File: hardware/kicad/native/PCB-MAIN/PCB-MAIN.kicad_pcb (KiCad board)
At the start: 6 copper layers, 110 x 75 mm, 251 parts, among them J10 U.FL-R-SMT-1(60), J11 USB4105-GF-A-120, J12 MEM2052-00-195-00-A, J13 504050-0291, J6 2336582-1, J7 2336582-1, J8 U.FL-R-SMT-1(60), J9 U.FL-R-SMT-1(60), Q1 MMBT3904,215, Q2 MMBT3904,215, Q3 MMBT3904,215, Q4 Si1016X-T1-GE3, U1 STM32U585VIT6Q, U10 E22-900M22S, U11 MDBT50Q-P1MV2, U13 TS3A27518EPWR, U14 ESDALC6V1-5P6, U15 ESDALC6V1-5P6, U16 SN74AXC8T245PWR, U17 SN74LVC32APWR, U18 SN74AXC1T45DRLR, U19 TPD4E05U06DQAR, U2 W25Q512JVFIQ, U20 TPD4E05U06DQAR, U21 TPD4E05U06DQAR, U22 TPD4E05U06DQAR, U23 TPD4E05U06DQAR, U24 TPD4E05U06DQAR, U25 TPD2EUSB30DRTR, U26 TPD2EUSB30DRTR, U27 TPD4E05U06DQAR, U3 LIS2DW12TR, U4 STTS22HTR, U5 LT6000IDCB#TRMPBF, U6 SN74LVC1G07DBVR, U7 SN74AXC8T245PWR, U8 BG95-M3, U9 MAX-M10S-00B, X1 SiT1552AI-JE-DCC-32.768D

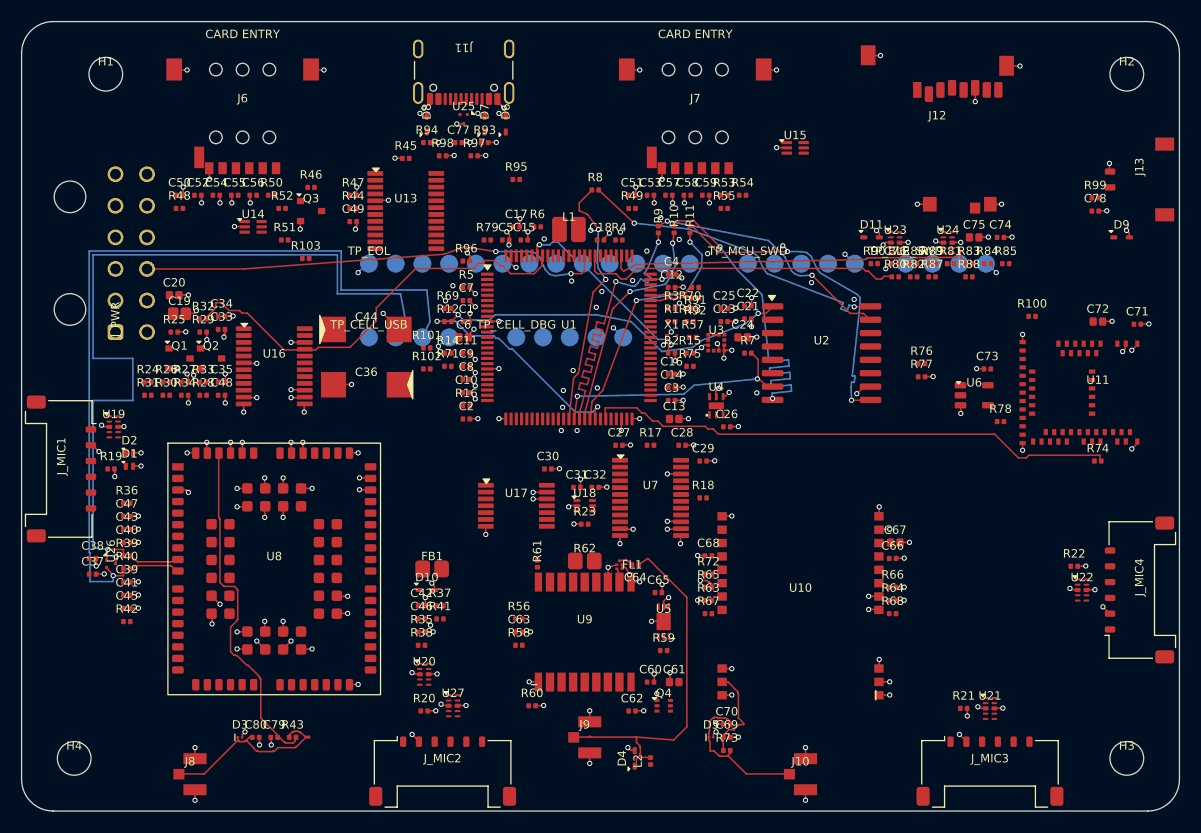
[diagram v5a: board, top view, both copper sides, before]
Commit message: Adopt PCB-MAIN 8-layer Rev.B EVT baseline
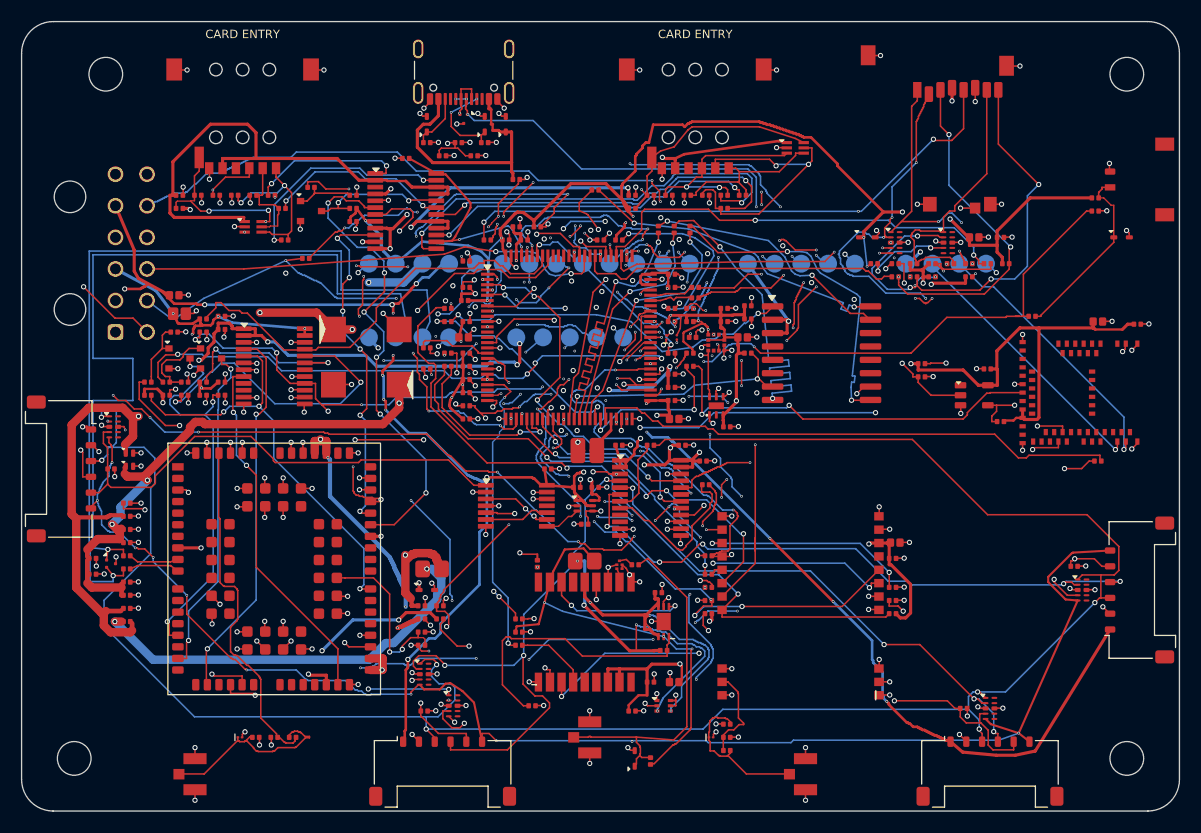
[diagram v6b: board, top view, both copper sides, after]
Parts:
- moved L1 21.1 mm to (53.8, 40.8)
- moved R18 1.27 mm to (65.0, 44.0)
- moved D11 0.40 mm to (80.3, 20.5)
- moved C7 0.15 mm to (42.1, 26.5), turned to 180 degrees
- turned R49 to 0 degrees
- renumbered J_PWR to J_PWR1, TP_BLE_SWD to TP_BLE_SWD1, TP_CELL_DBG to TP_CELL_DBG1, TP_CELL_USB to TP_CELL_USB1, TP_EOL to TP_EOL1, TP_MCU_SWD to TP_MCU_SWD1
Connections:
- C10 pad 1: VREF+ -> 3V3_DIGITAL
- C11 pad 1: VREF+ -> 3V3_DIGITAL
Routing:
- net 3V3_DIGITAL: track 0.00 -> 470.8 mm, vias 0 -> 42
- net PDM_CLK_1V8_FANOUT: track 0.00 -> 212.5 mm, vias 0 -> 7
- net 1V8_MIC: track 0.00 -> 207.4 mm, vias 0 -> 18
- net AAD_CFG_1V8_FANOUT: track 0.00 -> 170.6 mm, vias 0 -> 13
- net I2C2_SDA_BUS: track 0.00 -> 113.1 mm, vias 0 -> 6
- net CELL_PWRKEY_CMD: track 0.00 -> 108.3 mm, vias 0 -> 12
- net 3V8_MODEM_RF: track 0.00 -> 107.6 mm, vias 0 -> 7
- net 3V8_MODEM: track 0.00 -> 104.5 mm, vias 0 -> 3
- net U8_VDD_EXT_1V8: track 0.00 -> 98.1 mm, vias 0 -> 8
- net I2C2_SCL_BUS: track 0.00 -> 93.9 mm, vias 0 -> 9
- net 3V8_MODEM_BB: track 0.00 -> 93.0 mm, vias 0 -> 5
- net PDM_DATA1_1V8: track 0.00 -> 80.6 mm, vias 0 -> 10
- net PWR_GOOD: track 0.00 -> 80.1 mm, vias 0 -> 3
- net MIC_WAKE3: track 0.00 -> 77.7 mm, vias 0 -> 2
- net CELL_DBG_TXD_TP: track 0.00 -> 77.1 mm, vias 0 -> 4
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- added copper zone on In6.Cu, net GND_DIGITAL
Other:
- copper layers 6 -> 8
